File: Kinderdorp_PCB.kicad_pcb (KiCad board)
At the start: 2 copper layers, 40 parts, among them J1 Conn_01x08, Q1 2N7002_C306856, U2 AMS1117-3.3_C347222, U5 ESP32-C3-WROOM-02-N4(4MB)

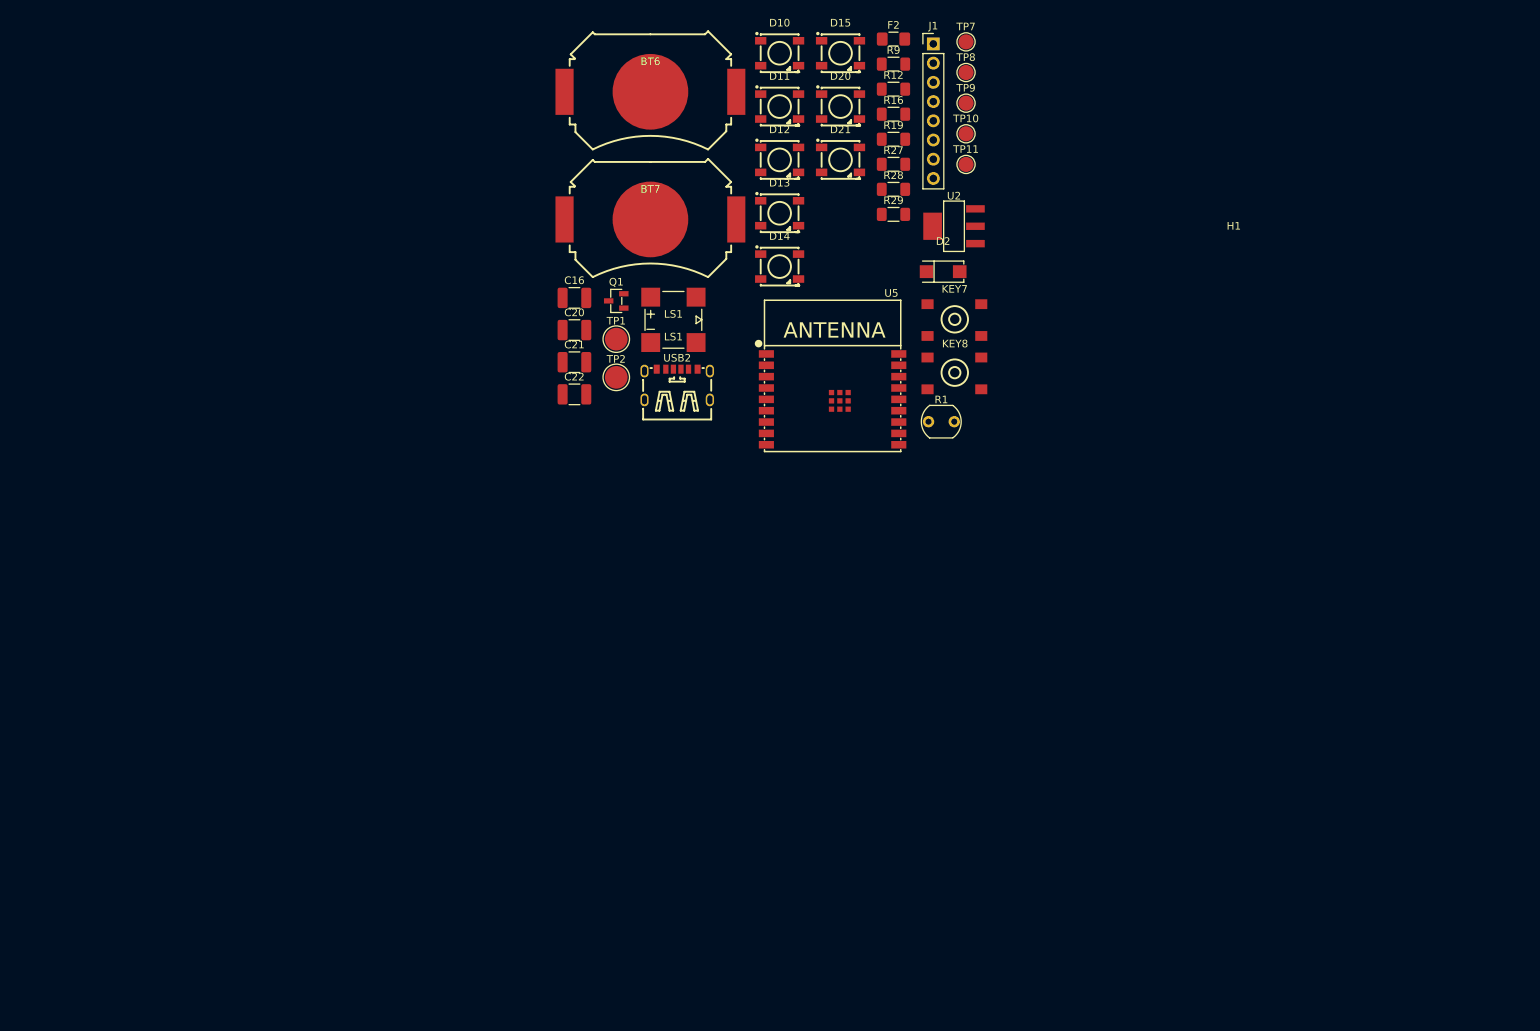
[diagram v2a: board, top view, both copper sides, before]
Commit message: imported/created thumb design
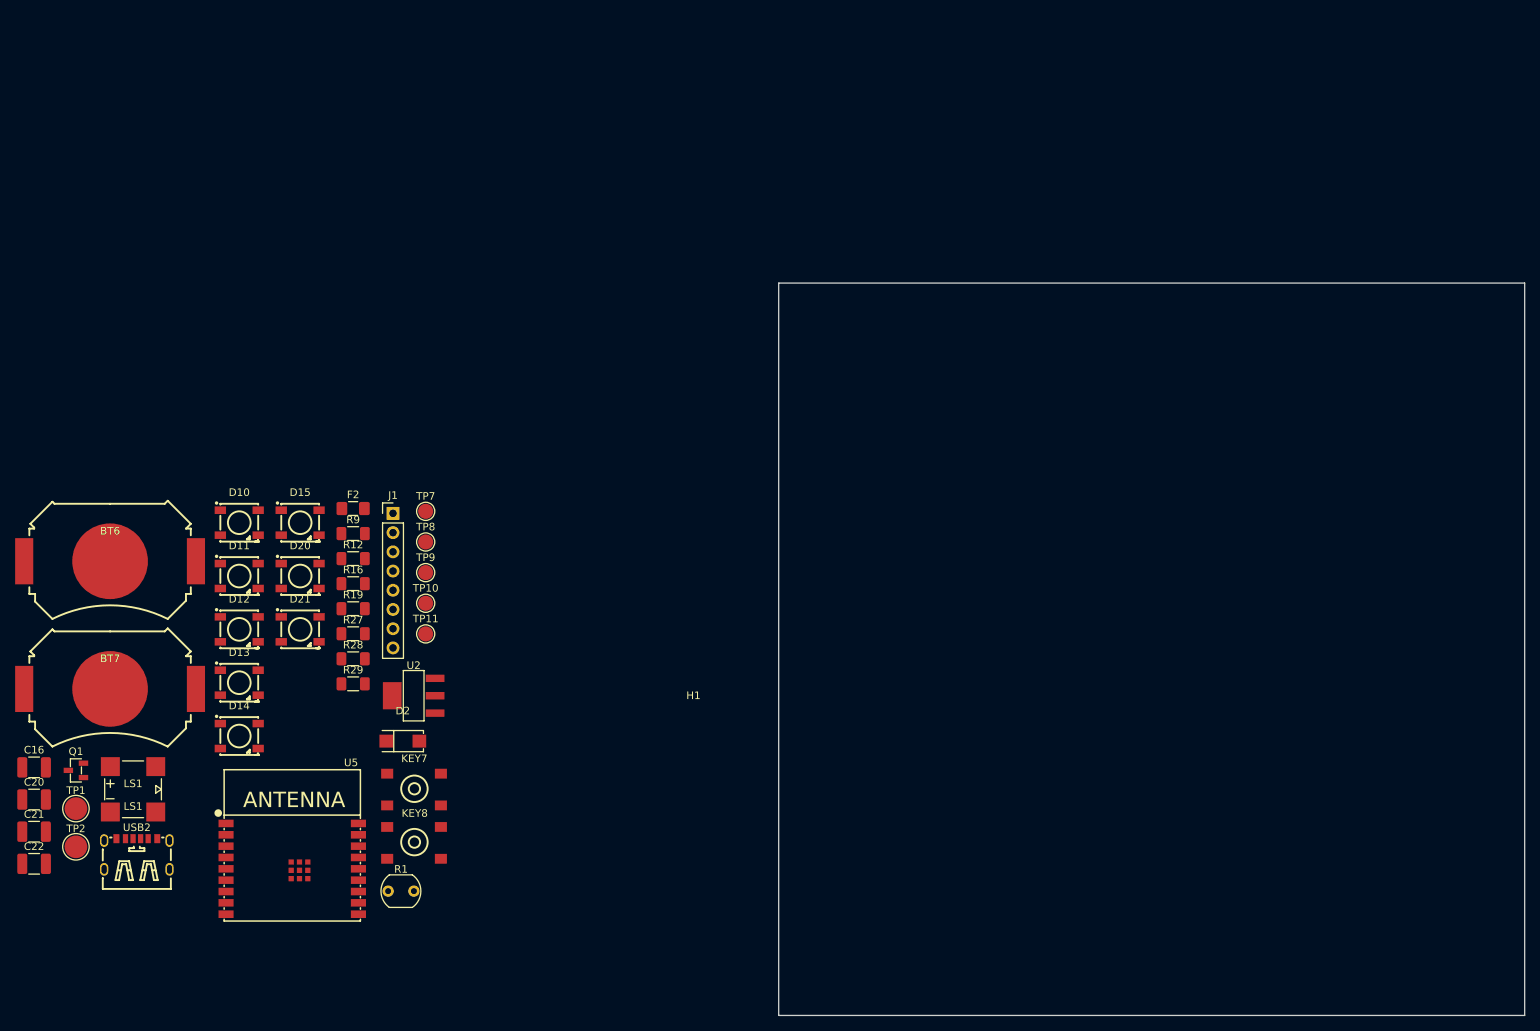
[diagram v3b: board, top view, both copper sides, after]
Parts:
- moved BT6 94.6 mm to (63.7, 102.3)
- moved BT7 94.6 mm to (63.7, 119.2)
- moved D15 94.6 mm to (88.8, 97.2)
- moved D2 94.6 mm to (102.4, 126.1)
- moved D20 94.6 mm to (88.8, 104.3)
- moved D21 94.6 mm to (88.8, 111.3)
- moved F2 94.6 mm to (95.8, 95.4)
- moved KEY7 94.6 mm to (103.9, 132.4)
- moved KEY8 94.6 mm to (104.0, 139.5)
- moved LS1 94.6 mm to (66.8, 132.2)
- moved R12 94.6 mm to (95.8, 102.0)
- moved R16 94.6 mm to (95.8, 105.3)
- moved R19 94.6 mm to (95.8, 108.6)
- moved R27 94.6 mm to (95.8, 111.9)
- moved R28 94.6 mm to (95.8, 115.2)
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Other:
- board outline added: 98.6 x 96.8 mm

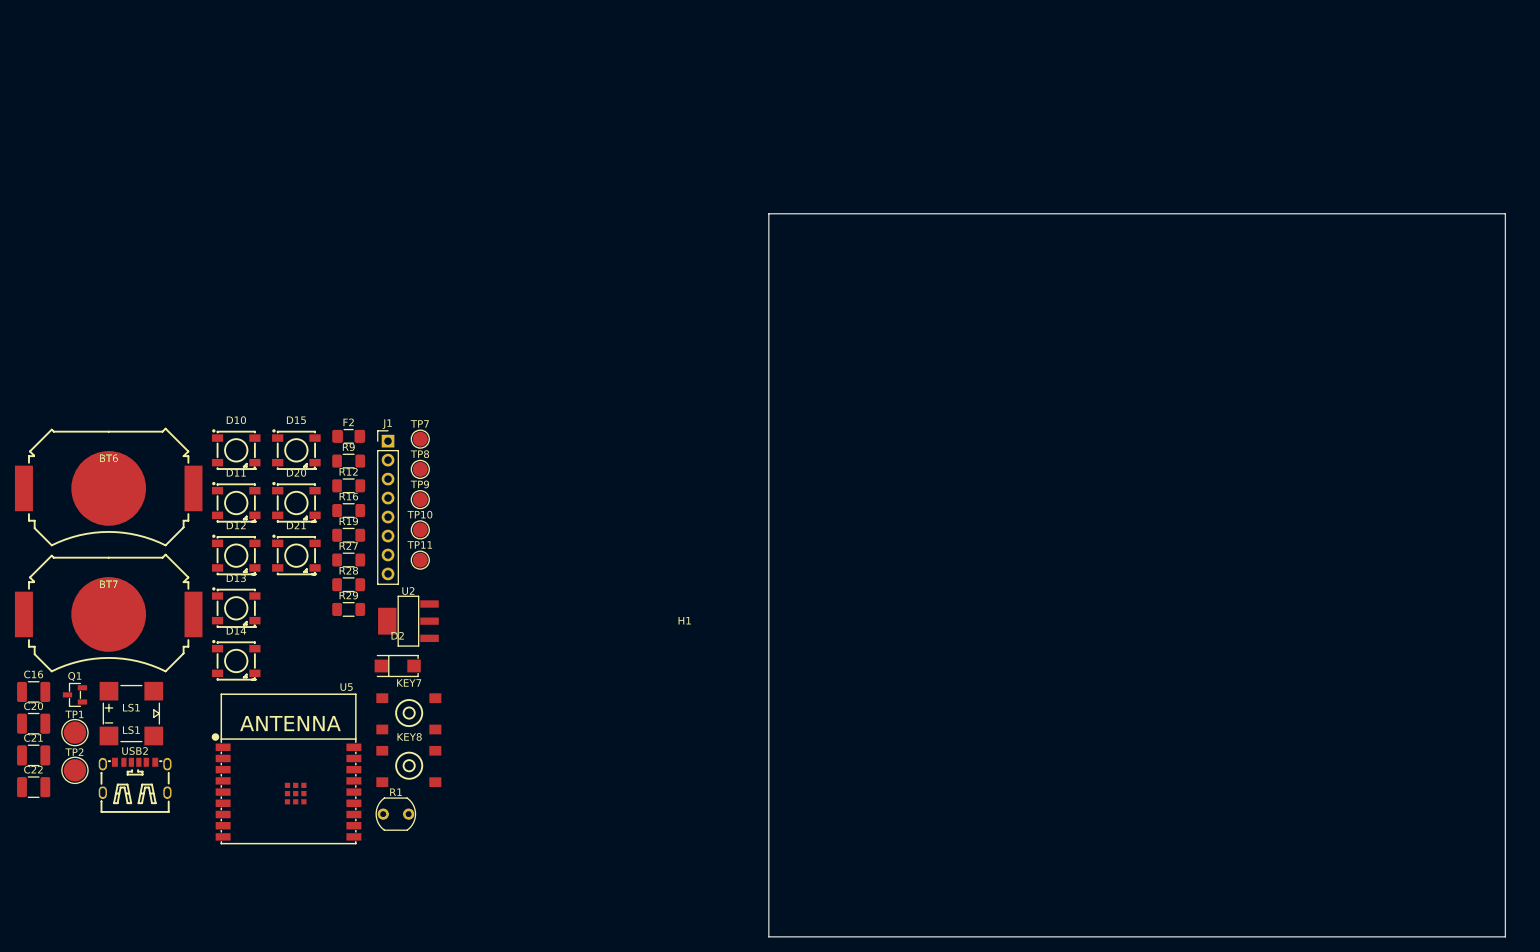
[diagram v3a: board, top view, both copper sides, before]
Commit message: created new oultine for pcb
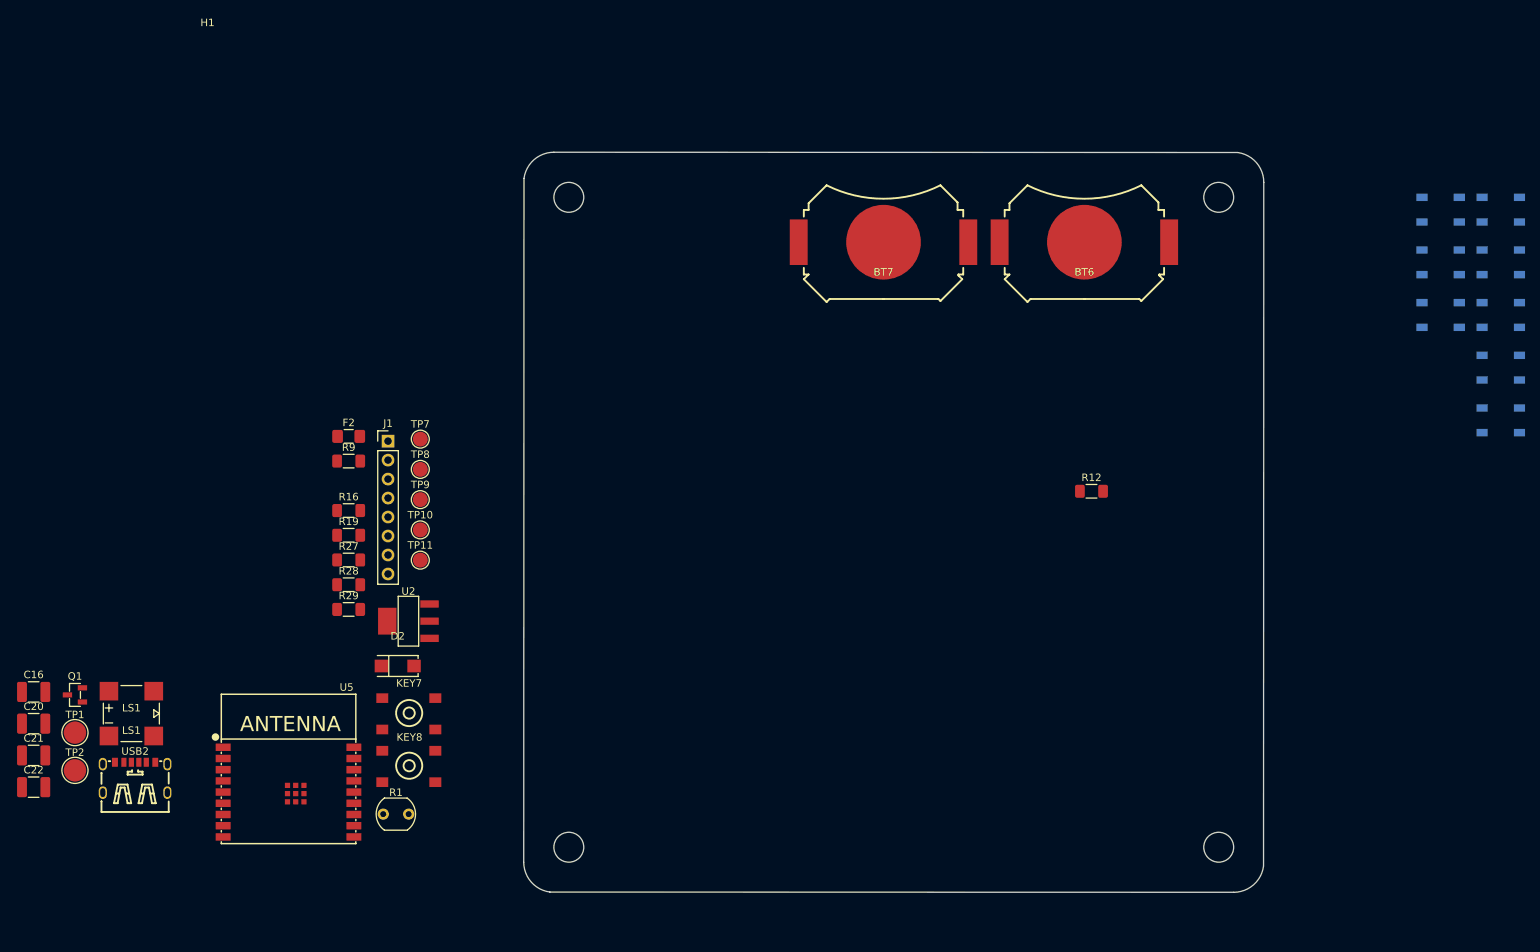
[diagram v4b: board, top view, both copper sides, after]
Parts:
- D10, D11, D12, D13, D14, D15, D20, D21: moved to B.Cu
- moved D10 172.3 mm to (250.1, 65.0), turned to 180 degrees
- moved D11 172.3 mm to (250.1, 72.1), turned to 180 degrees
- moved D12 172.3 mm to (250.1, 79.1), turned to 180 degrees
- moved D13 172.3 mm to (250.1, 86.2), turned to 180 degrees
- moved D14 172.3 mm to (250.1, 93.2), turned to 180 degrees
- moved D15 156.5 mm to (242.0, 65.0), turned to 180 degrees
- moved D20 156.5 mm to (242.0, 72.1), turned to 180 degrees
- moved D21 156.5 mm to (242.0, 79.1), turned to 180 degrees
- moved BT6 134.7 mm to (194.3, 69.4), turned to 180 degrees
- moved BT7 115.1 mm to (167.4, 69.4), turned to 180 degrees
- moved H1 102.5 mm to (77.0, 43.0)
- moved R12 99.4 mm to (195.3, 102.7)
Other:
- board size 98.6 x 96.8 mm -> 99.1 x 99.1 mm

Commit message: fixed naming designators
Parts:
- added R6: 10k, Resistor_SMD:R_1206_3216Metric_Pad1.30x1.75mm_HandSolder, F.Cu at (234.9, 118.3)
- added R7: 10k, Resistor_SMD:R_1206_3216Metric_Pad1.30x1.75mm_HandSolder, F.Cu at (234.9, 115.0)
- KEY1: renamed from KEY8; moved to B.Cu
- KEY2: renamed from KEY7; moved to B.Cu
- LS1: moved to B.Cu
- R10: renamed from R1; moved to B.Cu
- moved USB1 202.3 mm to (268.1, 116.6), turned to 90 degrees
- moved U2 159.6 mm to (247.0, 153.7), turned to 90 degrees
- moved F1 152.9 mm to (246.1, 123.8)
- moved R8 150.7 mm to (246.1, 130.4)
- moved R9 150.7 mm to (246.1, 127.1)
- moved D1 145.0 mm to (232.1, 61.2)
- moved BT2 119.9 mm to (74.8, 60.8)
- moved BT1 119.9 mm to (47.9, 60.8)
- moved KEY1 112.1 mm to (211.2, 107.0), turned to -90 degrees
- moved R10 106.0 mm to (195.1, 98.2), turned to 180 degrees
- moved LS1 94.8 mm to (150.9, 88.5), turned to 180 degrees
- moved J1 92.6 mm to (193.3, 104.6)
- moved R5 53.3 mm to (248.4, 106.6)
- moved KEY2 34.9 mm to (127.7, 106.9), turned to -90 degrees
- renumbered BT7 to BT1, BT6 to BT2, C20 to C1, C16 to C2, C21 to C3, C22 to C4, D2 to D1, D20 to D2, D15 to D3, D11 to D4, D13 to D5, D10 to D6, D21 to D7, D12 to D8, D14 to D9, F2 to F1, R9 to R1, R16 to R2, R19 to R3, R27 to R4, R12 to R5, R29 to R8, R28 to R9, TP10 to TP1, TP8 to TP2, TP9 to TP3, TP7 to TP4, TP11 to TP5, TP1 to TP6, TP2 to TP7, U2 to U1, U5 to U2, USB2 to USB1
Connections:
- KEY1 pad 3: GPIO5 -> GPIO4
- KEY1 pad 4: GPIO5 -> GPIO4
- KEY2 pad 3: GPIO4 -> GPIO5
- KEY2 pad 4: GPIO4 -> GPIO5
- U2 pad 18: GPIO0 -> BATT_V
- USB1 pad 7: GND -> unconnected-(USB2-EH-Pad7)_3

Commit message: fixed annotation again
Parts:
- HDR1: renamed from J1; moved to B.Cu
- moved LED5 126.6 mm to (147.7, 139.5), turned to 160 degrees
- moved LED4 126.3 mm to (129.5, 123.8)
- moved LED3 120.3 mm to (131.4, 92.0), turned to -135 degrees
- moved LED2 103.7 mm to (138.4, 64.6), turned to -135 degrees
- moved U1 91.3 mm to (193.7, 136.7)
- moved LED6 87.8 mm to (180.4, 141.6), turned to -160 degrees
- moved U2 78.1 mm to (170.2, 139.2), turned to 180 degrees
- moved LED7 64.3 mm to (208.4, 128.1), turned to 135 degrees
- moved USB1 59.7 mm to (212.3, 137.9)
- moved LED1 54.7 mm to (188.0, 63.7), turned to 135 degrees
- moved BT1 43.2 mm to (91.1, 60.5), turned to 0 degrees
- moved LED8 39.6 mm to (210.6, 95.8), turned to -135 degrees
- moved BT2 23.2 mm to (91.1, 77.4), turned to 0 degrees
- moved HDR1 9.31 mm to (202.6, 104.1), turned to 180 degrees
- moved LDR1 8.44 mm to (187.9, 93.8)
- renumbered KEY1 to BUTTON1, KEY2 to BUTTON2, R10 to LDR1, D2 to LED1, D3 to LED2, D4 to LED3, D5 to LED4, D6 to LED5, D7 to LED6, D8 to LED7, D9 to LED8
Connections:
- BT1 pad 1: Net-(BT6-Pad2) -> /Net-(D2-A)
- BT1 pad 2: GND -> Net-(BT6-Pad2)
- BT2 pad 1: Net-(D2-A) -> Net-(BT6-Pad2)
- BT2 pad 2: Net-(BT6-Pad2) -> GND
- D1 pad 1: Net-(D2-C) -> Net-(D1-C)
- D1 pad 2: Net-(D2-A) -> /Net-(D2-A)
- LDR1 pad 2: Net-(U5-IO2) -> /Net-(U5-IO2)
- R7 pad 1: Net-(D2-A) -> /Net-(D2-A)
- TP6 pad 1: Net-(D2-A) -> /Net-(D2-A)
- U2 pad 11: Net-(U5-RXD) -> /Net-(U5-RXD)
- U2 pad 12: Net-(U5-TXD) -> /Net-(U5-TXD)
- U2 pad 16: Net-(U5-IO2) -> Net-(U2-IO2)
- USB1 pad A5: Net-(USB2-CC1) -> Net-(USB1-CC1)
- USB1 pad A9: Net-(D2-C) -> Net-(D1-C)
- USB1 pad B5: Net-(USB2-CC2) -> Net-(USB1-CC2)
- USB1 pad B9: Net-(D2-C) -> Net-(D1-C)

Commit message: finished layout
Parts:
- removed H1: Batteryplaceholder, MountingHole:MountingHole_2.1mm
- removed TP1, TP2: TestPoint_Probe, TestPoint:TestPoint_Pad_D2.0mm
- added BATT+: ~, TestPoint:TestPoint_Pad_D3.0mm, F.Cu at (208.6, 120.3)
- added BATT-: TestPoint_Alt, TestPoint:TestPoint_Pad_D3.0mm, F.Cu at (214.7, 120.3)
- added BATTPACK1:: Batteryplaceholder, MountingHole:MountingHole_2.1mm, F.Cu at (139.6, 98.9)
- C1: value 100nF 50V -> 47uF 10V
- C2: value 47uF 10V -> 100nF 50V
- GND: renamed from TP7; value TestPoint_Alt -> TestPoint_Probe; footprint TestPoint:TestPoint_Pad_D3.0mm -> TestPoint:TestPoint_Pad_D2.0mm
- R2: value 5k -> 10k
- R3: value 200 -> 5k1
- R4: value 10k -> 5k1
- R5: value 200 -> 5k
- R6: value 10k -> 200
- R8: value 5k1 -> 10k
- R9: value 5k1 -> 200
- TXD: renamed from TP6; value ~ -> TestPoint_Probe; footprint TestPoint:TestPoint_Pad_D3.0mm -> TestPoint:TestPoint_Pad_D2.0mm
- moved C1 139.7 mm to (193.4, 134.6), turned to 180 degrees
- moved C3 134.5 mm to (187.8, 148.5), turned to 90 degrees
- moved C2 130.9 mm to (183.2, 148.5), turned to -90 degrees
- moved C4 129.4 mm to (183.1, 141.6), turned to -90 degrees
- moved R4 114.8 mm to (205.8, 144.9), turned to 90 degrees
- moved R3 112.4 mm to (205.8, 131.9), turned to -90 degrees
- moved USB- 109.9 mm to (214.3, 110.5)
- moved USB+ 104.0 mm to (209.2, 110.5)
- moved R9 96.7 mm to (149.8, 136.8), turned to 90 degrees
- moved BT1: 95.1 mm to (178.7, 97.7), turned to 180 degrees
- moved R8 93.1 mm to (153.2, 136.8), turned to -90 degrees
- moved Q1 92.2 mm to (151.4, 130.9), turned to -90 degrees
- moved R6 86.7 mm to (152.1, 143.6)
- moved GND 85.0 mm to (143.5, 151.0)
- moved TXD 81.7 mm to (139.3, 151.0)
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- renumbered BT1 to BT1:, BT2 to BT2:, LED5 to LED1, LED4 to LED2, LED2 to LED4, LED1 to LED5, LED8 to LED6, LED6 to LED8, TP5 to RXD, TP3 to USB+, TP4 to USB-
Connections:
- BT1: pad 1: /Net-(D2-A) -> Net-(D1-A)
- C1 pad 1: +3V3 -> GND
- C1 pad 2: GND -> +5V
- C2 pad 1: GND -> +3V3
- C2 pad 2: +5V -> GND
- D1 pad 2: /Net-(D2-A) -> Net-(D1-A)
- F1 pad 2: Net-(D2-C) -> Net-(D1-C)
- LDR1 pad 2: /Net-(U5-IO2) -> Net-(U2-IO2)
- LED1 pad 2: Net-(D10-DOUT) -> Net-(LED1-DOUT)
- LED1 pad 4: Net-(D10-DIN) -> Net-(LED1-DIN)
- LED2 pad 2: Net-(D13-DOUT) -> Net-(LED2-DOUT)
- LED2 pad 4: Net-(D12-DOUT) -> Net-(LED1-DOUT)
- LED3 pad 2: Net-(D11-DOUT) -> Net-(LED3-DOUT)
- LED3 pad 4: Net-(D10-DOUT) -> Net-(LED2-DOUT)
- LED4 pad 2: Net-(D15-DOUT) -> Net-(LED4-DOUT)
- LED4 pad 4: Net-(D14-DOUT) -> Net-(LED3-DOUT)
- LED5 pad 2: unconnected-(D20-DOUT-Pad2) -> Net-(LED5-DOUT)
- LED5 pad 4: Net-(D20-DIN) -> Net-(LED4-DOUT)
- LED6 pad 2: Net-(D14-DOUT) -> Net-(LED6-DOUT)
- LED6 pad 4: Net-(D13-DOUT) -> Net-(LED5-DOUT)
- LED7 pad 2: Net-(D12-DOUT) -> Net-(LED7-DOUT)
- LED7 pad 4: Net-(D11-DOUT) -> Net-(LED6-DOUT)
- LED8 pad 2: Net-(D20-DIN) -> unconnected-(LED8-DOUT-Pad2)
- LED8 pad 4: Net-(D15-DOUT) -> Net-(LED7-DOUT)
- R1 pad 1: GND -> Net-(D1-A)
- R1 pad 2: BUZZ -> BATT_V
- R2 pad 1: Net-(U5-IO2) -> BATT_V
- R3 pad 1: BUZZ -> GND
- R3 pad 2: Net-(Q1-G) -> Net-(USB1-CC2)
- R4 pad 1: +3V3 -> GND
- R4 pad 2: ESP_EN -> Net-(USB1-CC1)
- R5 pad 1: Net-(D10-DIN) -> Net-(U2-IO2)
- R5 pad 2: GPIO3 -> GND
- R6 pad 1: BATT_V -> Net-(LED1-DIN)
- R6 pad 2: GND -> GPIO3
- R7 pad 1: /Net-(D2-A) -> +3V3
- R7 pad 2: BATT_V -> ESP_EN
- R8 pad 2: Net-(USB2-CC2) -> BUZZ
- R9 pad 1: GND -> BUZZ
- R9 pad 2: Net-(USB2-CC1) -> Net-(Q1-G)
- RXD pad 1: GND -> Net-(U2-RXD)
- TXD pad 1: /Net-(D2-A) -> Net-(U2-TXD)
- U2 pad 11: /Net-(U5-RXD) -> Net-(U2-RXD)
- U2 pad 12: /Net-(U5-TXD) -> Net-(U2-TXD)
- USB+ pad 1: Net-(U5-TXD) -> D+_USB
- USB- pad 1: D+_USB -> D-_USB
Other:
- board text added: "3.3V"
- board text added: "5V->3.3V"
- board text added: "AAA"
- board text added: "BATTERY_V"
- board text added: "BUZZER_CTRL"
- board text added: "CR2032"
- board text added: "GND"
- board text added: "GPIO HDR"
- board text added: "INT"
- board text added: "LDR+R"
- board text added: "MICRO-PROCESSOR"
- board text added: "NC"
- board text added: "Programming"
- board text added: "SCL"
- board text added: "SDA"
- board text added: "SDO"
- board text added: "UART"

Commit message: updated logo
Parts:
- added G***: LOGO, LOGO, F.Cu at (127.8, 79.4)
- added G***: LOGO, LOGO, F.Cu at (198.2, 71.9)
- moved USB- 45.0 mm to (171.9, 125.7)
- moved USB+ 45.0 mm to (166.8, 125.7)
- moved D1 2.57 mm to (201.8, 134.1)
- moved R6 2.35 mm to (154.3, 143.1)
- moved F1 2.29 mm to (200.0, 140.3)
- moved R4 1.83 mm to (207.3, 143.9)
- moved R3 1.50 mm to (207.3, 131.8)
- moved LDR1 0.79 mm to (198.9, 92.0)
- moved R5 0.79 mm to (197.1, 97.1)
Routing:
- net Net-(D1-A): track 0.00 -> 140.3 mm
- net +3V3: track 0.00 -> 83.4 mm
- net Net-(BT1-Pad2): track 0.00 -> 61.0 mm
- net Net-(Q1-D): track 0.00 -> 39.6 mm, vias 0 -> 1
- net BATT_V: track 0.00 -> 37.2 mm
- net D-_USB: track 0.00 -> 23.7 mm
- net Net-(D1-C): track 0.00 -> 21.4 mm
- net D+_USB: track 0.00 -> 17.1 mm
- net +5V: track 0.00 -> 14.4 mm
- net Net-(LED1-DIN): track 0.00 -> 14.0 mm, vias 0 -> 1
- net BUZZ: track 0.00 -> 13.9 mm
- net Net-(USB1-CC1): track 0.00 -> 12.2 mm
- net Net-(USB1-CC2): track 0.00 -> 12.2 mm
- net ESP_EN: track 0.00 -> 9.25 mm
- net GPIO3: track 0.00 -> 6.59 mm
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- added copper zone on B.Cu, net GND
- added copper zone on F.Cu, net GND
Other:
- board text added: "Casper R. Tak 26-07-2025 https://github.com/Casperdroid5/Kinderdorp-PCB"
- board text added: "MICRO-PROCESSOR (MCU)"
- board text added: "Power"
- board text added: "Protection"
- board text added: "USB-C (15W)"
- board text removed: "MICRO-PROCESSOR"
